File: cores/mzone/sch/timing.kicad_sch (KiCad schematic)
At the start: 41 parts

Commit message: mzone core
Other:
- note added: "48"
- note removed: "not correct symbol?!"

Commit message: mzone core
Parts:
- added unit 5 of C12
- added unit 5 of C13
- added unit 3 of G6
- renumbered C13 to CC13
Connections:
- net GND: now also C12.7 (GND), C13.7 (GND), G6.7 (GND)
- net V1: no longer B12.9 (~{PE}), B13.9 (~{PE}), B14.2
- net VCC: now also C12.14 (VCC), C13.14 (VCC), G6.14 (VCC)
- new net: B12.9 (~{PE}), B13.9 (~{PE}), B14.2
- no-connect marks 40 -> 41
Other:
- moved on the sheet: G4H

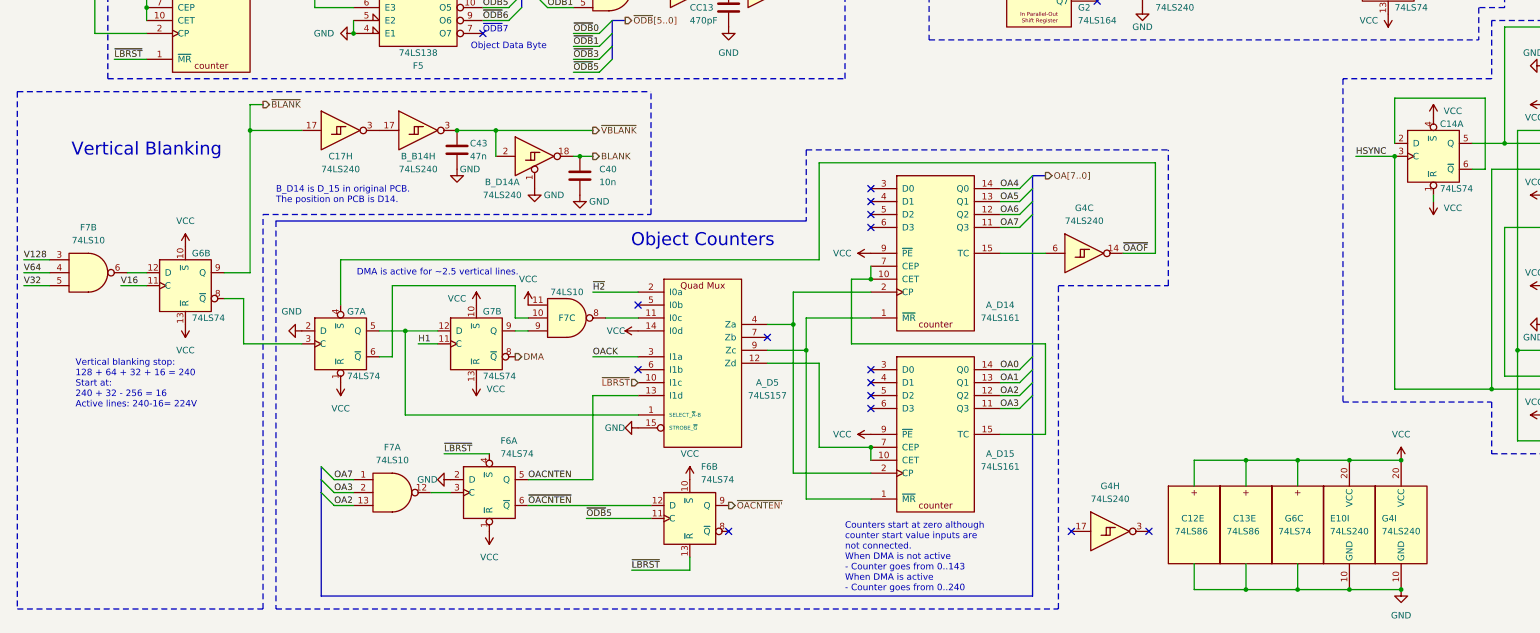
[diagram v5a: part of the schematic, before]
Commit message: mzone core
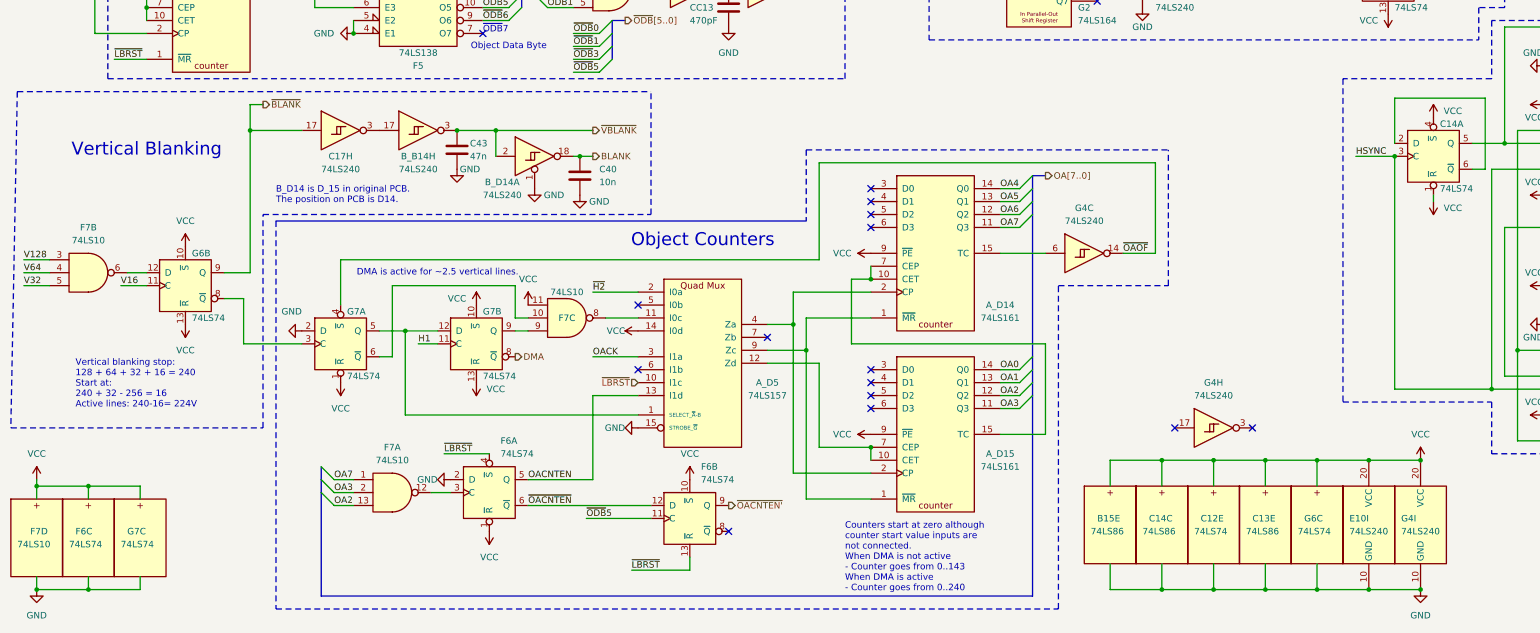
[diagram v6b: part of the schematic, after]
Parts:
- added unit 5 of B15
- added unit 3 of C14
- added unit 3 of F6
- added unit 4 of F7
- added unit 3 of G7
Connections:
- net GND: now also B15.7 (GND), C14.7 (GND), F6.7 (GND), F7.7 (GND), G7.7 (GND)
- net VCC: now also B15.14 (VCC), C14.14 (VCC), F6.14 (VCC), F7.14 (VCC), G7.14 (VCC)
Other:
- moved on the sheet: C12E, C13E, E10I, G4H, G4I, G6C

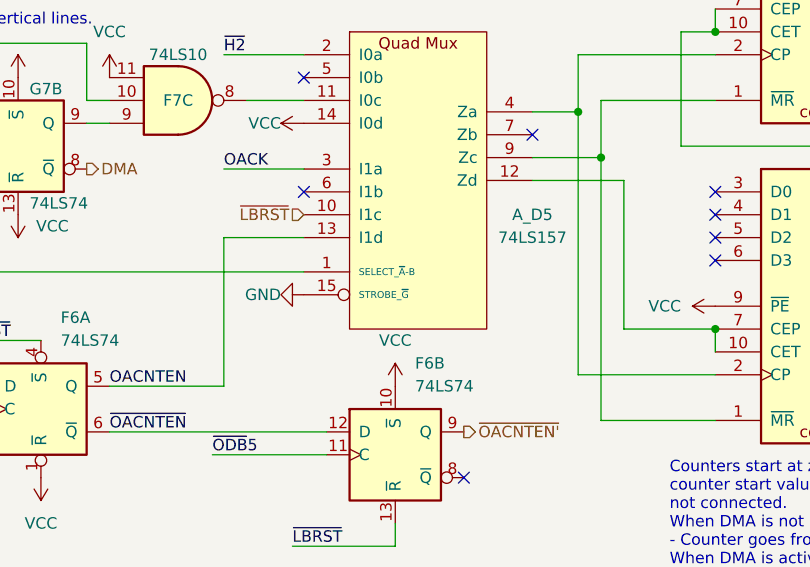
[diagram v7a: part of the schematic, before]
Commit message: mzone core
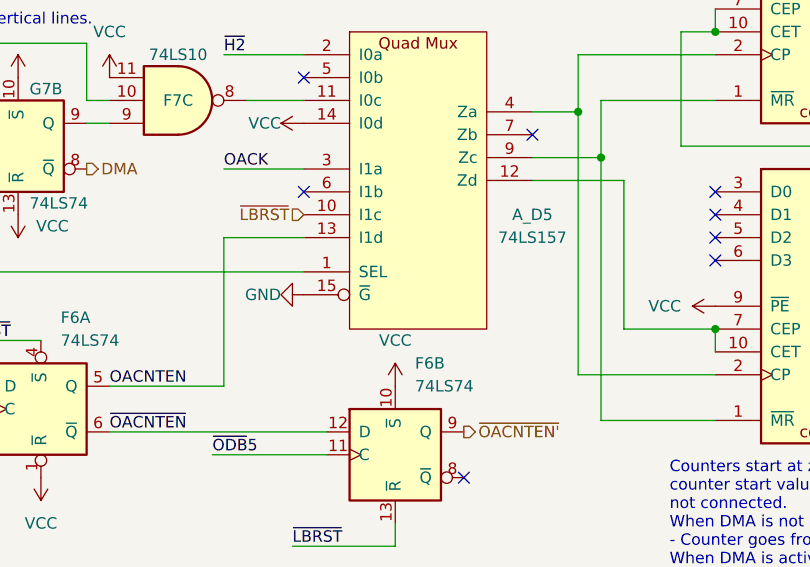
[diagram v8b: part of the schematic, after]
